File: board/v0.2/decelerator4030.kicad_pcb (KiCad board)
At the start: 2 copper layers, 71 parts, among them CON1 A3000/A4000_LOCAL_BUS_SLOT, J3 XILINX_JTAG, J4 CONN_2, J5 CONN_4, U1 MC68030FE, U10 74LXC245, U11 74LXC245, U12 MCP9801, U13 DS1086L, U14 XTAL_OSC_DIP8, U15 MCP1826S, U16 IS66WVE4M16, U17 IS66WVE4M16, U18 MC68030RC_PGA, U19 XC9536XL-5VQG44C, U2 XC95144XL-10TQG144C, U3 AS6C3216, U4 AS6C3216, U5 S29AL016J, U6 S29AL016J, U7 PCA9564, U8 74LXC245, U9 74LXC245

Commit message: Some change boards and schematic
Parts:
- C10: moved to B.Cu
- U18: value MC68030RC_PGA -> MC68030FE_PGA
- moved C26 32.2 mm to (179.2, 65.4), turned to 270 degrees
- moved U16 30.1 mm to (175.1, 65.5), turned to 180 degrees
- moved C23 29.0 mm to (215.9, 65.5), turned to 270 degrees
- moved C24 28.9 mm to (170.9, 65.5), turned to 90 degrees
- moved U17 22.0 mm to (211.9, 65.5), turned to 180 degrees
- moved C32 18.8 mm to (53.0, 92.2)
- moved C25 15.2 mm to (207.9, 65.4), turned to 90 degrees
- moved C30 13.9 mm to (48.2, 107.5)
- moved C31 10.3 mm to (44.7, 97.3), turned to 270 degrees
- moved C10 8.99 mm to (161.5, 65.6), turned to 90 degrees
- moved C8 7.51 mm to (159.7, 48.5), turned to 270 degrees
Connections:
- U16 pad A3: /ARM0 -> /ARM5
- U16 pad A4: /ARM1 -> /ARM3
- U16 pad A5: /ARM2 -> /ARM1
- U16 pad B3: /ARM3 -> /ARM6
- U16 pad B4: /ARM4 -> /ARM2
- U16 pad C1: /DRM9 -> /DRM10
- U16 pad C2: /DRM10 -> /DRM9
- U16 pad C3: /ARM5 -> /ARM7
- U16 pad C4: /ARM6 -> /ARM0
- U16 pad D3: /ARM17 -> /ARM4
- U16 pad D4: /ARM7 -> /ARM21
- U16 pad E3: /ARM21 -> /ARM17
- U16 pad E4: /ARM16 -> /ARM12
- U16 pad F1: /DRM14 -> /DRM13
- U16 pad F2: /DRM13 -> /DRM14
- U16 pad F3: /ARM14 -> /ARM8
- U16 pad F4: /ARM15 -> /ARM20
- U16 pad F5: /DRM5 -> /DRM6
- U16 pad F6: /DRM6 -> /DRM5
- U16 pad G2: /ARM19 -> /ARM18
- U16 pad G3: /ARM12 -> /ARM10
- U16 pad G4: /ARM13 -> /ARM14
- U16 pad H1: /ARM18 -> /ARM19
- U16 pad H2: /ARM8 -> /ARM9
- U16 pad H3: /ARM9 -> /ARM11
- U16 pad H4: /ARM10 -> /ARM13
- U16 pad H5: /ARM11 -> /ARM15
- U16 pad H6: /ARM20 -> /ARM16
- U17 pad A3: /ARM0 -> /ARM5
- U17 pad A4: /ARM1 -> /ARM3
- U17 pad A5: /ARM2 -> /ARM1
- U17 pad B3: /ARM3 -> /ARM6
- U17 pad B4: /ARM4 -> /ARM2
- U17 pad C3: /ARM5 -> /ARM7
- U17 pad C4: /ARM6 -> /ARM0
- U17 pad D3: /ARM17 -> /ARM4
- U17 pad D4: /ARM7 -> /ARM21
- U17 pad E3: /ARM21 -> /ARM17
- U17 pad E4: /ARM16 -> /ARM12
- U17 pad F3: /ARM14 -> /ARM8
- U17 pad F4: /ARM15 -> /ARM20
- U17 pad G2: /ARM19 -> /ARM18
- U17 pad G3: /ARM12 -> /ARM10
- U17 pad G4: /ARM13 -> /ARM14
- U17 pad H1: /ARM18 -> /ARM19
- U17 pad H2: /ARM8 -> /ARM9
- U17 pad H3: /ARM9 -> /ARM11
- U17 pad H4: /ARM10 -> /ARM13
- U17 pad H5: /ARM11 -> /ARM15
- U17 pad H6: /ARM20 -> /ARM16
- U19 pad 12: /A23 -> /A27
- U19 pad 13: /A24 -> /A26
- U19 pad 16: /A26 -> /A24
- U19 pad 18: /A27 -> /A23
- U19 pad 19: /A28 -> /A22
- U19 pad 20: /A29 -> /A21
- U19 pad 21: /A30 -> /A20
- U19 pad 22: /A31 -> /A19
- U19 pad 5: /A19 -> /A31
- U19 pad 6: /A20 -> /A30
- U19 pad 7: /A21 -> /A29
- U19 pad 8: /A22 -> /A28
- U2 pad 124: _I2CINT -> _I2CCE
- U2 pad 125: _I2CCE -> _I2CINT
- U2 pad 39: /A4 -> MA24
- U2 pad 40: /A10 -> MA25
- U2 pad 41: /A5 -> MA26
- U2 pad 43: /A12 -> /A31
- U2 pad 44: /A6 -> /A30
- U2 pad 45: /A13 -> /A29
- U2 pad 46: /A9 -> /A28
- U2 pad 48: /A11 -> /A27
- U2 pad 49: /A14 -> /A23
- U2 pad 50: /A15 -> /A22
- U2 pad 51: /A16 -> /A18
- U2 pad 52: /A17 -> /A21
- U2 pad 53: /A19 -> /A20
- U2 pad 54: /A20 -> /A16
- U2 pad 56: /A22 -> /A19
- U2 pad 57: /A23 -> /A11
- U2 pad 58: MA25 -> /A14
- U2 pad 59: /A18 -> /A17
- U2 pad 60: MA26 -> /A9
- U2 pad 61: /A28 -> /A12
- U2 pad 64: /A29 -> /A15
- U2 pad 66: /A21 -> /A6
- U2 pad 68: MA24 -> /A13
- U2 pad 69: /A30 -> /A5
- U2 pad 70: /A27 -> /A10
- U2 pad 71: /A31 -> /A4
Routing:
- net TDO2: track 0.00 -> 181.5 mm, vias 0 -> 3
- net TDO1: track 0.00 -> 116.3 mm, vias 0 -> 4
- net _MAPEN: track 0.00 -> 108.1 mm, vias 0 -> 2
- net LOGIC_CLK: track 46.3 -> 149.5 mm, vias 0 -> 2
- net TCK: track 65.8 -> 167.1 mm, vias 3 -> 4
- net TMS: track 62.1 -> 161.8 mm, vias 3 -> 4
- net SCL: track 25.5 -> 105.5 mm, vias 2 -> 4
- net SDA: track 27.5 -> 105.8 mm, vias 2 -> 4
- net N-00000177: track 0.00 -> 66.1 mm, vias 0 -> 2
- net _ECS: track 81.8 -> 143.9 mm
- net +3.3V: track 118.9 -> 177.0 mm, vias 0 -> 4
- net 68030CLK: track 115.7 -> 164.5 mm, vias 2 -> 4
- net MA24: track 68.1 -> 108.2 mm
- net /ARM21: track 0.00 -> 40.0 mm, vias 0 -> 2
- net MA25: track 72.4 -> 108.5 mm
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
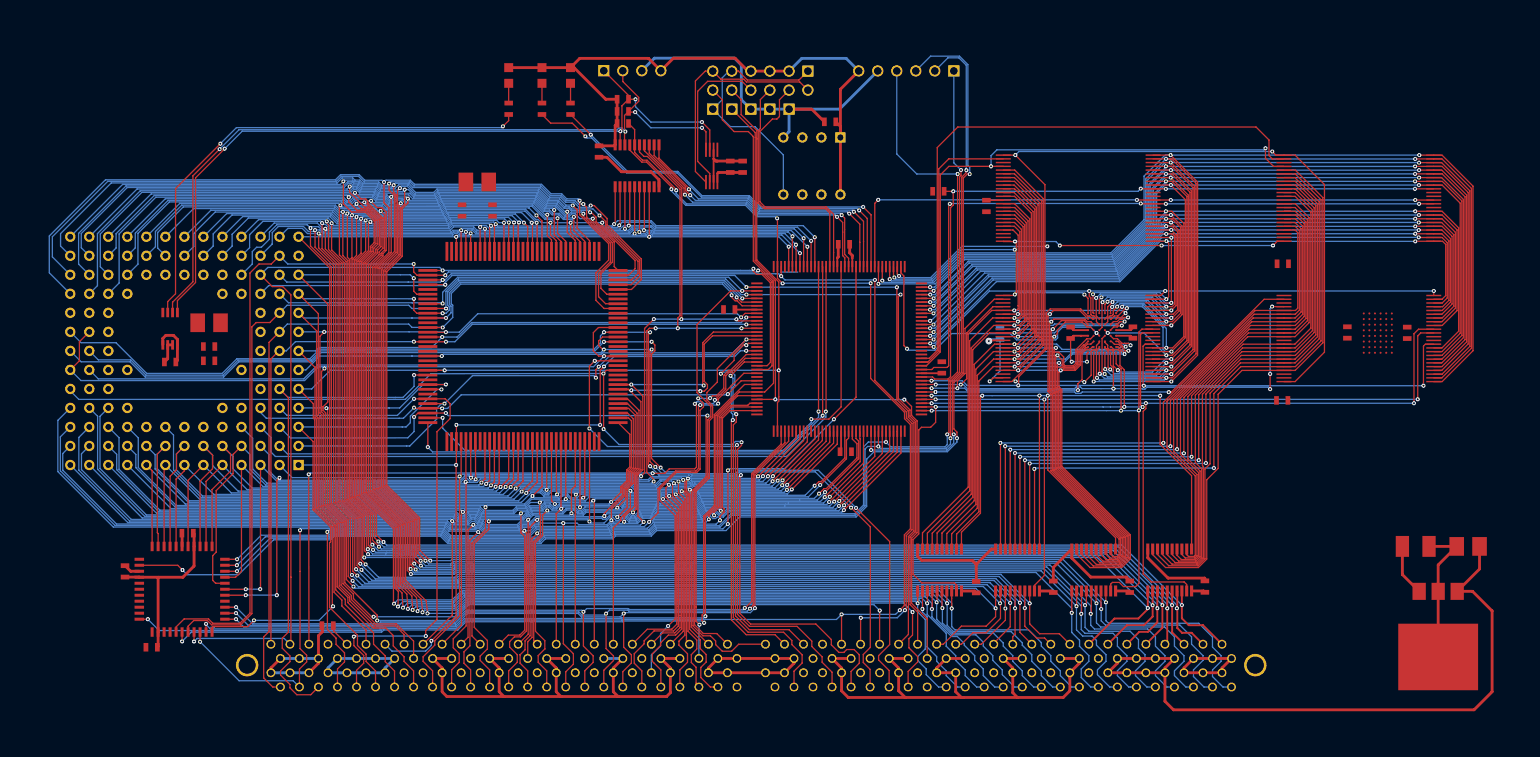
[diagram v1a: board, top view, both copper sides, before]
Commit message: Fixed bug pin numbering of CON1
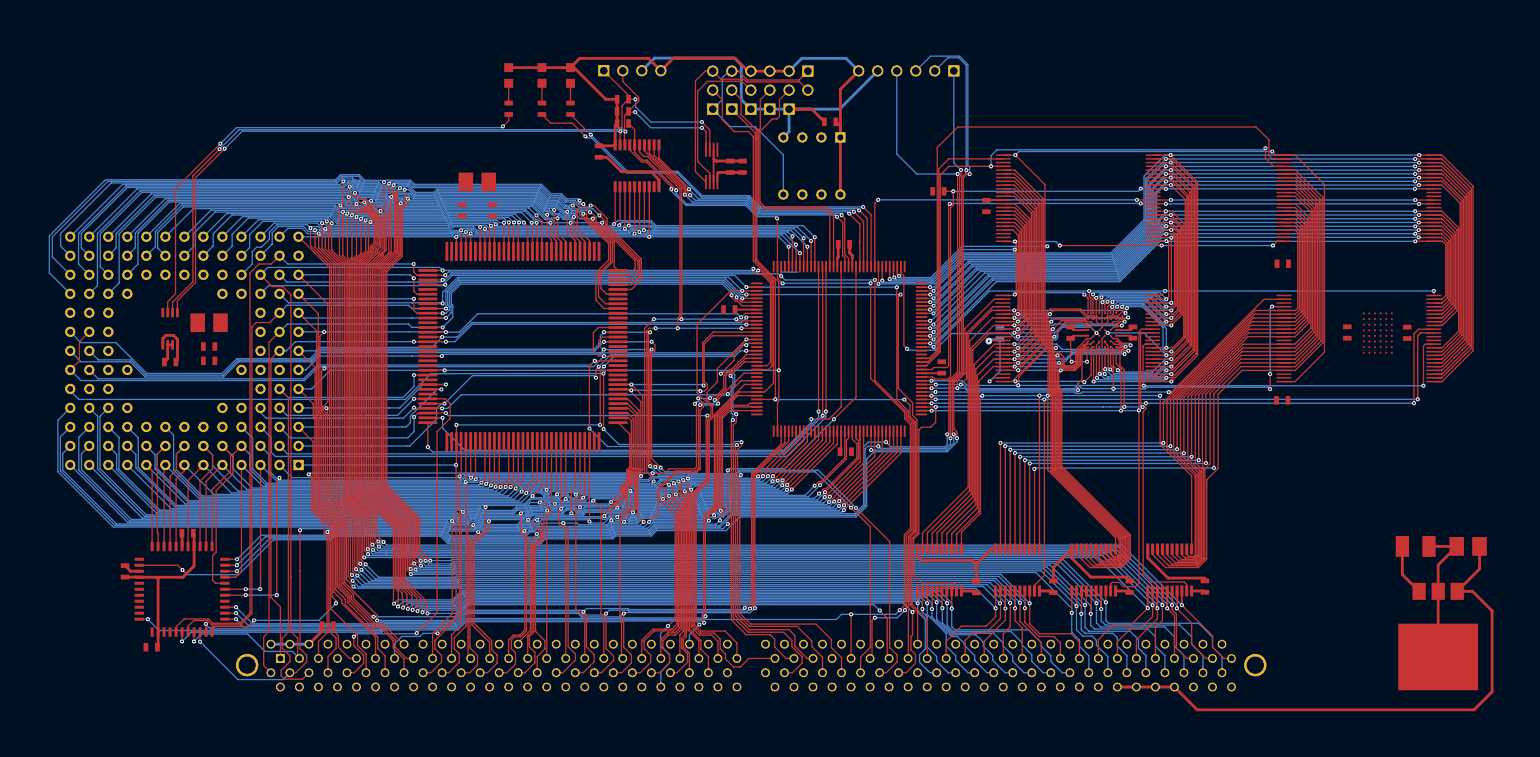
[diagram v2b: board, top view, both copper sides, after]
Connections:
- CON1 pad 59: GND -> (no net)
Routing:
- net GND: track 320.2 -> 148.1 mm
- net +5V: track 138.1 -> 76.1 mm
- net /IPL0: track 157.5 -> 152.5 mm
- net R_W: track 151.1 -> 155.7 mm
- net /D3: track 263.4 -> 259.3 mm
- net /D6: track 262.2 -> 258.0 mm
- net /D5: track 257.7 -> 253.7 mm
- net /D2: track 265.1 -> 261.0 mm
- net /D4: track 264.8 -> 260.7 mm
- net /D7: track 258.2 -> 254.2 mm
- net /D1: track 255.5 -> 251.5 mm
- net /D0: track 265.9 -> 262.0 mm
- net _EMUL: track 134.9 -> 131.0 mm
- net /A31: track 137.6 -> 133.8 mm
- net _SBR: track 95.7 -> 99.0 mm
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
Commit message: semifinal board prototype
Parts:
- added C33: 100nF, SM0603_Capa, B.Cu at (100.1, 66.0)
- added C34: 100nF, SM0603_Capa, F.Cu at (131.7, 53.8)
- added C35: 100nF, SM0603_Capa, F.Cu at (148.0, 53.7)
- added C36: 100nF, SM0603_Capa, F.Cu at (128.8, 81.1)
- added C37: 100nF, SM0603_Capa, B.Cu at (149.8, 78.2)
- added C38: 100nF, SM0603_Capa, B.Cu at (133.0, 78.4)
- added C39: 100nF, SM0603_Capa, F.Cu at (126.2, 58.0)
- added U20: MCP9801, MSOP-8, B.Cu at (97.5, 64.4)
- C11, C2, C3: moved to B.Cu
- U18: value MC68030FE_PGA -> MC68030RC_PGA
- moved C2 32.4 mm to (98.9, 76.9)
- moved C3 13.8 mm to (106.5, 54.4), turned to 180 degrees
- moved C27 11.6 mm to (45.0, 63.2), turned to 270 degrees
- moved C11 8.91 mm to (199.4, 65.6), turned to 90 degrees
- moved C9 8.05 mm to (197.0, 48.5), turned to 270 degrees
- moved C29 6.14 mm to (53.9, 75.0), turned to 180 degrees
- moved C1 2.32 mm to (87.6, 50.3)
- moved C30 0.28 mm to (48.2, 107.7), turned to 180 degrees
- turned C31 to 90 degrees
- turned C32 to 180 degrees
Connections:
- net CIOUT renamed N-000001
- net TDI renamed N-00000155
- C30 pad 1: GND -> +3.3V
- C30 pad 2: +3.3V -> GND
- C31 pad 1: GND -> +3.3V
- C31 pad 2: +3.3V -> GND
- C32 pad 1: GND -> +3.3V
- C32 pad 2: +3.3V -> GND
- CON1 pad 59: (no net) -> GND
- U17 pad C1: /DRM25 -> /DRM26
- U17 pad C2: /DRM26 -> /DRM25
- U17 pad F1: /DRM30 -> /DRM29
- U17 pad F2: /DRM29 -> /DRM30
- U17 pad F5: /DRM21 -> /DRM22
- U17 pad F6: /DRM22 -> /DRM21
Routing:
- net +3.3V: track 177.0 -> 800.1 mm, vias 4 -> 39
- net GND: track 148.1 -> 747.1 mm, vias 0 -> 114
- net +5V: track 76.1 -> 663.8 mm, vias 0 -> 6
- net /ARM21: track 40.0 -> 89.9 mm, vias 2 -> 7
- net N-00000142: track 66.1 -> 102.7 mm, vias 2 -> 6
- net SCL: track 105.5 -> 141.6 mm, vias 4 -> 8
- net SDA: track 105.8 -> 140.7 mm, vias 4 -> 8
- net _SRAM_HI_CE: track 53.7 -> 87.3 mm, vias 2 -> 3
- net _SRAM_OE: track 78.4 -> 105.6 mm, vias 6 -> 5
- net /ARM16: track 78.6 -> 102.4 mm, vias 8 -> 10
- net /DRM31: track 76.6 -> 97.3 mm, vias 2 -> 4
- net /DRM28: track 80.9 -> 101.2 mm, vias 2 -> 4
- net /DRM30: track 78.0 -> 97.9 mm, vias 2 -> 4
- net /DRM29: track 79.4 -> 98.3 mm, vias 2 -> 4
- net /DRM26: track 84.4 -> 102.9 mm, vias 2 -> 4
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- added copper zone on B.Cu, net GND
- added copper zone on F.Cu, net GND

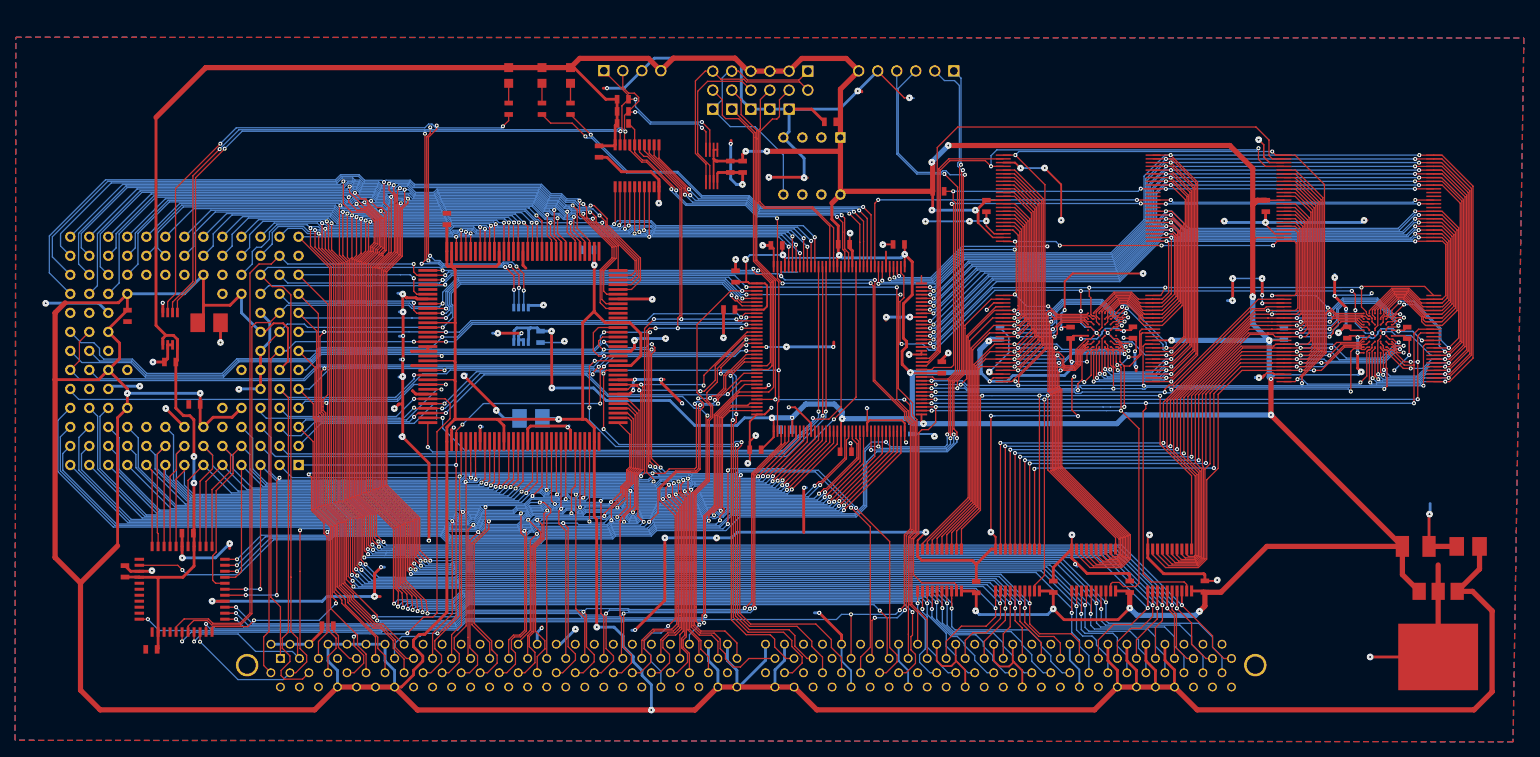
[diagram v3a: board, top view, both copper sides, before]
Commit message: Revert the mistaken revert.
This reverts commit 6991797e6b54a4bce98f1816d85600409aecea96.
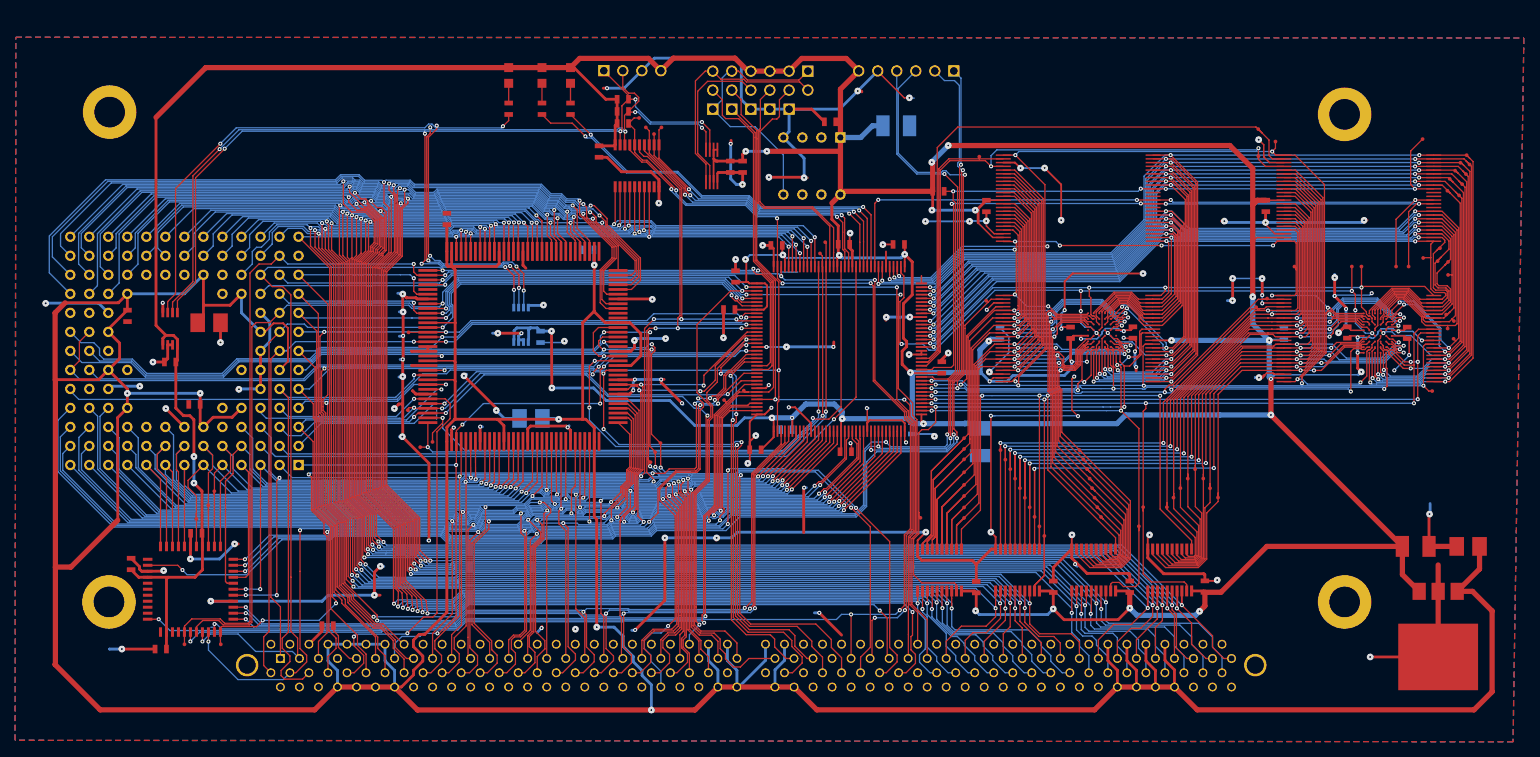
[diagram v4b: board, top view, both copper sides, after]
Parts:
- added ?: , PINTST_0.5, F.Cu at (161.6, 81.1)
- added ?: , PINTST_0.5, F.Cu at (167.4, 92.6)
- added ?: , PINTST_0.5, F.Cu at (175.0, 90.1)
- added ?: , PINTST_0.5, F.Cu at (174.5, 88.8)
- added ?: , PINTST_0.5, F.Cu at (174.1, 87.5)
- added ?: , PINTST_0.5, F.Cu at (173.8, 86.2)
- added ?: , PINTST_0.5, F.Cu at (173.5, 85.0)
- added ?: , PINTST_0.5, F.Cu at (173.1, 83.7)
- added ?: , PINTST_0.5, F.Cu at (172.6, 82.4)
- added ?: , PINTST_0.5, F.Cu at (172.1, 81.1)
- added ?: , PINTST_0.5, F.Cu at (180.0, 91.3)
- added ?: , PINTST_0.5, F.Cu at (162.2, 82.4)
- added ?: , PINTST_0.5, F.Cu at (180.6, 88.8)
- added ?: , PINTST_0.5, F.Cu at (183.8, 88.8)
- added ?: , PINTST_0.5, F.Cu at (184.7, 87.5)
- added ?: , PINTST_0.5, F.Cu at (185.6, 86.2)
- added ?: , PINTST_0.5, F.Cu at (186.6, 84.9)
- added ?: , PINTST_0.5, F.Cu at (187.5, 83.7)
- added ?: , PINTST_0.5, F.Cu at (188.6, 84.9)
- added ?: , PINTST_0.5, F.Cu at (189.5, 86.2)
- added ?: , PINTST_0.5, F.Cu at (190.6, 87.5)
- added ?: , PINTST_0.5, F.Cu at (156.7, 79.6)
- added ?: , PINTST_0.5, F.Cu at (162.9, 83.7)
- added ?: , PINTST_0.5, F.Cu at (156.7, 81.0)
- added ?: , PINTST_0.5, F.Cu at (156.7, 82.4)
- added ?: , PINTST_0.5, F.Cu at (156.7, 84.1)
- added ?: , PINTST_0.5, F.Cu at (156.7, 85.8)
- added ?: , PINTST_0.5, F.Cu at (156.7, 87.3)
- added ?: , PINTST_0.5, F.Cu at (156.7, 88.8)
- added ?: , PINTST_0.5, F.Cu at (156.7, 90.2)
- added ?: , PINTST_0.5, F.Cu at (150.9, 90.2)
- added ?: , PINTST_0.5, F.Cu at (209.8, 56.6)
- added ?: , PINTST_0.5, F.Cu at (208.5, 56.6)
- added ?: , PINTST_0.5, F.Cu at (163.5, 85.0)
- added ?: , PINTST_0.5, F.Cu at (200.8, 56.6)
- added ?: , PINTST_0.5, F.Cu at (198.3, 39.9)
- added ?: , PINTST_0.5, F.Cu at (223.8, 41.8)
- added ?: , PINTST_0.5, F.Cu at (224.2, 43.0)
- added ?: , PINTST_0.5, F.Cu at (223.0, 42.8)
- added ?: , PINTST_0.5, F.Cu at (223.7, 44.3)
- added ?: , PINTST_0.5, F.Cu at (222.3, 43.8)
- added ?: , PINTST_0.5, F.Cu at (223.2, 45.6)
- added ?: , PINTST_0.5, F.Cu at (221.5, 44.9)
- added ?: , PINTST_0.5, F.Cu at (222.8, 47.1)
- added ?: , PINTST_0.5, F.Cu at (164.1, 86.2)
- added ?: , PINTST_0.5, F.Cu at (221.2, 46.5)
- added ?: , PINTST_0.5, F.Cu at (221.3, 64.9)
- added ?: , PINTST_0.5, F.Cu at (222.1, 63.9)
- added ?: , PINTST_0.5, F.Cu at (221.1, 63.0)
- added ?: , PINTST_0.5, F.Cu at (218.0, 55.5)
- added ?: , PINTST_0.5, F.Cu at (220.2, 54.2)
- added ?: , PINTST_0.5, F.Cu at (219.9, 55.9)
- added ?: , PINTST_0.5, F.Cu at (221.3, 56.0)
- added ?: , PINTST_0.5, F.Cu at (221.3, 57.7)
- added ?: , PINTST_0.5, F.Cu at (196.0, 41.9)
- added ?: , PINTST_0.5, F.Cu at (164.8, 87.5)
- added ?: , PINTST_0.5, F.Cu at (196.0, 38.3)
- added ?: , PINTST_0.5, F.Cu at (197.2, 60.9)
- added ?: , PINTST_0.5, F.Cu at (195.7, 62.1)
- added ?: , PINTST_0.5, F.Cu at (219.2, 73.3)
- added ?: , PINTST_0.5, F.Cu at (216.1, 56.6)
- added ?: , PINTST_0.5, F.Cu at (214.4, 56.6)
- added ?: , PINTST_0.5, F.Cu at (217.9, 39.6)
- added ?: , PINTST_0.5, F.Cu at (158.7, 42.0)
- added ?: , PINTST_0.5, F.Cu at (159.6, 61.2)
- added ?: , PINTST_0.5, F.Cu at (113.3, 36.8)
- added ?: , PINTST_0.5, F.Cu at (165.5, 88.8)
- added ?: , PINTST_0.5, F.Cu at (114.2, 38.0)
- added ?: , PINTST_0.5, F.Cu at (115.3, 38.9)
- added ?: , PINTST_0.5, F.Cu at (116.3, 38.0)
- added ?: , PINTST_0.5, F.Cu at (127.3, 73.2)
- added ?: , PINTST_0.5, F.Cu at (124.7, 74.5)
- added ?: , PINTST_0.5, F.Cu at (85.7, 80.0)
- added ?: , PINTST_0.5, F.Cu at (84.1, 80.7)
- added ?: , PINTST_0.5, F.Cu at (137.5, 54.9)
- added ?: , PINTST_0.5, F.Cu at (138.2, 53.4)
- added ?: , PINTST_0.5, F.Cu at (114.8, 82.8)
- added ?: , PINTST_0.5, F.Cu at (166.1, 90.1)
- added ?: , PINTST_0.5, F.Cu at (115.4, 81.4)
- added ?: , PINTST_0.5, F.Cu at (116.2, 80.2)
- added ?: , PINTST_0.5, F.Cu at (54.2, 90.3)
- added ?: , PINTST_0.5, F.Cu at (55.8, 88.5)
- added ?: , PINTST_0.5, F.Cu at (56.6, 86.6)
- added ?: , PINTST_0.5, F.Cu at (57.4, 107.1)
- added ?: , PINTST_0.5, F.Cu at (52.6, 107.1)
- added ?: , PINTST_0.5, F.Cu at (82.4, 75.8)
- added ?: , PINTST_0.5, F.Cu at (82.5, 65.4)
- added ?: , PINTST_0.5, F.Cu at (222.1, 66.3)
- added ?: , PINTST_0.5, F.Cu at (166.8, 91.3)
- added C40: 1uF, SM1210L, B.Cu at (158.9, 80.1)
- added C41: 1uF, SM1210L, B.Cu at (147.6, 37.8)
- added Hole_4mm: P***, hole_4mm, F.Cu at (207.5, 101.4)
- added Hole_4mm: P***, hole_4mm, F.Cu at (207.5, 36.3)
- added Hole_4mm: P***, hole_4mm, F.Cu at (42.6, 36.0)
- added Hole_4mm: P***, hole_4mm, F.Cu at (42.5, 101.4)
- moved C31 1.28 mm to (45.5, 96.3)
- moved C30 1.24 mm to (49.4, 107.7)
- moved C32 1.16 mm to (54.2, 92.2)
- moved U19 1.12 mm to (53.4, 99.7)
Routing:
- net GND: track 747.1 -> 695.8 mm, vias 114 -> 112
- net /DRM15: track 69.0 -> 85.4 mm
- net /DRM14: track 72.9 -> 88.3 mm
- net /DRM13: track 73.0 -> 85.5 mm
- net +3.3V: track 800.1 -> 812.4 mm
- net /DRM12: track 75.4 -> 87.2 mm
- net _RESET_CPLD: track 83.6 -> 93.5 mm
- net /DRM11: track 75.7 -> 85.5 mm
- net _FLASH_WE: track 90.6 -> 99.7 mm
- net /DRM10: track 74.5 -> 82.6 mm
- net _IDBUS_UUB: track 108.2 -> 116.1 mm
- net _FLASH_BUSY: track 94.8 -> 102.4 mm
- net /DRM24: track 104.8 -> 111.3 mm
- net /DRM9: track 77.9 -> 84.1 mm
- net (no net): track 10.5 -> 16.7 mm, vias 1 -> 4
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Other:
- board text added: "By: strim_ jarob asman"
- board text added: "Decelerator 4030 Proto v1.0"
- board text added: "SAKURA"
